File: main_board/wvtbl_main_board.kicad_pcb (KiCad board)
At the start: 2 copper layers, 29 x 110 mm, 11 parts, among them J101 V/Oct, J102 X, J103 Y, J104 Out, J105 Conn_02x08_Odd_Even

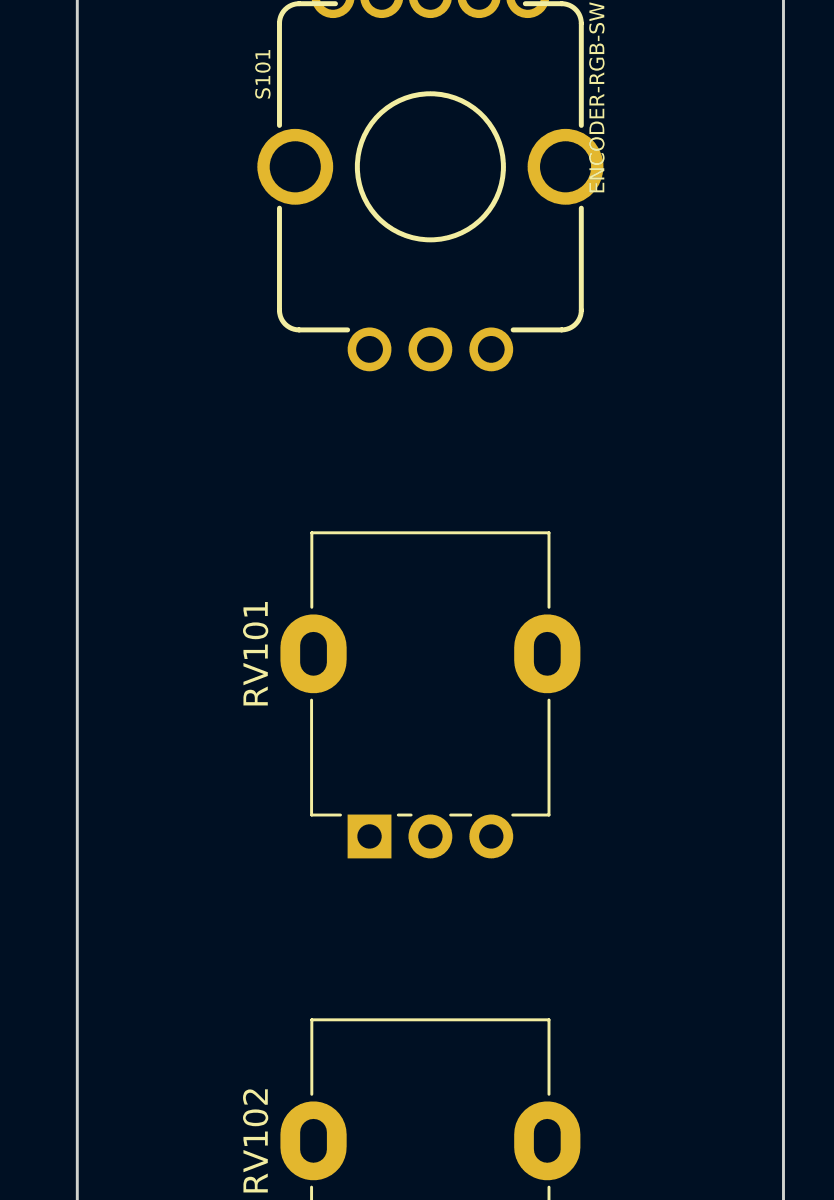
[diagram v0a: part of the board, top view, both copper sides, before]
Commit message: 6HP Compute module
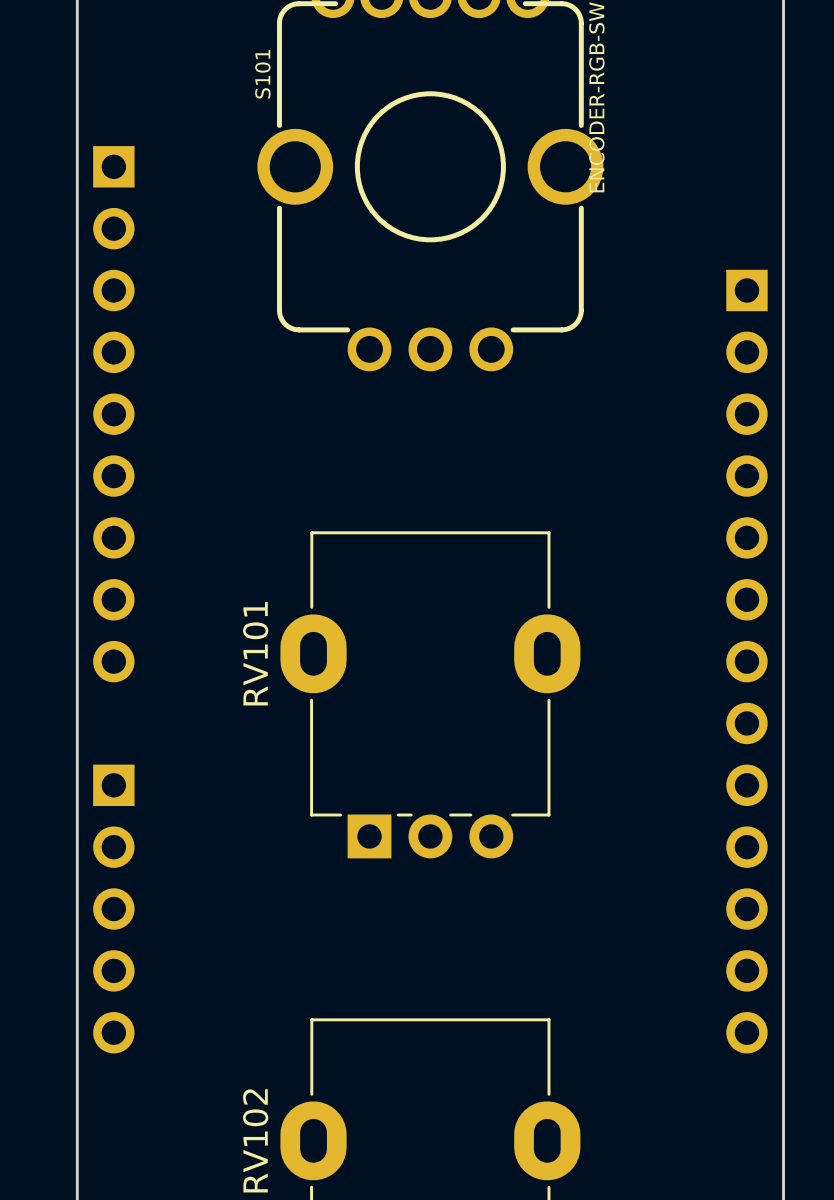
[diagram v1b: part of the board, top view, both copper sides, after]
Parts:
- added U101: CMPT6HP, WITNS:CMPT6HP, B.Cu at (50.0, 55.0)

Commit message: Main board PCB
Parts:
- removed J102: X, WITNS:Jack_3.5mm_QingPu_WQP-PJ398SM_Vertical_CircularHoles
- removed J103: Y, WITNS:Jack_3.5mm_QingPu_WQP-PJ398SM_Vertical_CircularHoles
- removed RV102, RV103, RV104: 100k, WITNS:Potentiometer_Alpha_RD901F-40-00D_Single_Vertical
- added C1: 10nF, Capacitor_SMD:C_0603_1608Metric, B.Cu at (44.0, 61.9)
- added C10: 10uF, Capacitor_SMD:CP_Elec_4x5.4, B.Cu at (42.0, 88.0)
- added C11: 100nF, Capacitor_SMD:C_0603_1608Metric, B.Cu at (45.8, 128.0)
- added C12: 10uF, Capacitor_SMD:CP_Elec_4x5.4, B.Cu at (42.0, 81.0)
- added C13: 100nF, Capacitor_SMD:C_0603_1608Metric, B.Cu at (50.8, 128.0)
- added C2: 100nF, Capacitor_SMD:C_0603_1608Metric, B.Cu at (50.8, 79.6)
- added C3: 100nF, Capacitor_SMD:C_0603_1608Metric, B.Cu at (59.0, 50.8)
- added C4: 10nF, Capacitor_SMD:C_0603_1608Metric, B.Cu at (51.6, 67.0)
- added C5: 100nF, Capacitor_SMD:C_0603_1608Metric, B.Cu at (50.8, 99.7)
- added C6: 100nF, Capacitor_SMD:C_0603_1608Metric, B.Cu at (43.3, 119.7)
- added C7: 100nF, Capacitor_SMD:C_0603_1608Metric, B.Cu at (58.2, 119.7)
- added C8: 10uF, Capacitor_SMD:CP_Elec_4x5.4, B.Cu at (38.0, 96.0)
- added C9: 100nF, Capacitor_SMD:C_0603_1608Metric, B.Cu at (50.8, 152.0)
- added D1: TVS 15V, Diode_SMD:D_SMA, B.Cu at (39.4, 144.0)
- added D2: TVS 15V, Diode_SMD:D_SMA, B.Cu at (39.4, 129.0)
- added D3: TVS 15V, Diode_SMD:D_SMA, B.Cu at (60.6, 144.0)
- added D4: TVS 15V, Diode_SMD:D_SMA, B.Cu at (60.6, 129.0)
- added J3: X, WITNS:Jack_3.5mm_QingPu_WQP-PJ398SM_Vertical_CircularHoles, F.Cu at (42.5, 132.0)
- added J4: Y, WITNS:Jack_3.5mm_QingPu_WQP-PJ398SM_Vertical_CircularHoles, F.Cu at (57.5, 132.0)
- added R1: 10k, Resistor_SMD:R_0603_1608Metric, B.Cu at (44.0, 59.9)
- added R2: 10k, Resistor_SMD:R_0603_1608Metric, B.Cu at (51.6, 65.0)
- added R3: 10k, Resistor_SMD:R_0603_1608Metric, B.Cu at (47.5, 59.0)
- added R4: 10k, Resistor_SMD:R_0603_1608Metric, B.Cu at (52.5, 59.0)
- added R5: 10k, Resistor_SMD:R_0603_1608Metric, B.Cu at (50.0, 51.0)
- added R6: 100R, Resistor_SMD:R_0603_1608Metric, B.Cu at (40.0, 66.8)
- added R7: 100R, Resistor_SMD:R_0603_1608Metric, B.Cu at (41.5, 66.8)
- added R8: 100R, Resistor_SMD:R_0603_1608Metric, B.Cu at (40.5, 72.8)
- added RV2: 100k, WITNS:Potentiometer_Alpha_RD901F-40-00D_Single_Vertical, F.Cu at (50.0, 95.0)
- added RV3: 100k, WITNS:Potentiometer_Alpha_RD901F-40-00D_Single_Vertical, F.Cu at (42.5, 115.0)
- added RV4: 100k, WITNS:Potentiometer_Alpha_RD901F-40-00D_Single_Vertical, F.Cu at (57.5, 115.0)
- J1: renamed from J105; value Conn_02x08_Odd_Even -> POWER
- renumbered J101 to J2, J104 to J5, RV101 to RV1, S101 to S1, U101 to U1
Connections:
- J1 pad 10: unconnected-(J105-Pad10) -> GND
- J1 pad 11: unconnected-(J105-Pad11) -> GND
- J1 pad 12: unconnected-(J105-Pad12) -> GND
- J1 pad 13: unconnected-(J105-Pad13) -> GND
- J1 pad 14: unconnected-(J105-Pad14) -> GND
- J1 pad 15: unconnected-(J105-Pad15) -> -12V
- J1 pad 16: unconnected-(J105-Pad16) -> -12V
- J1 pad 5: unconnected-(J105-Pad5) -> +5V
- J1 pad 6: unconnected-(J105-Pad6) -> +5V
- J1 pad 7: unconnected-(J105-Pad7) -> +12V
- J1 pad 8: unconnected-(J105-Pad8) -> +12V
- J1 pad 9: unconnected-(J105-Pad9) -> GND
- J2 pad S: unconnected-(J101-PadS) -> GND
- J2 pad T: unconnected-(J101-PadT) -> /CV1
- J2 pad TN: unconnected-(J101-PadTN) -> GND
- J5 pad S: unconnected-(J104-PadS) -> GND
- J5 pad T: unconnected-(J104-PadT) -> /OUT
- RV1 pad 1: unconnected-(RV101-Pad1) -> +3.3VA
- RV1 pad 2: unconnected-(RV101-Pad2) -> /POT_1
- RV1 pad 3: unconnected-(RV101-Pad3) -> GND
- S1 pad 1: unconnected-(S101-Pad1) -> Net-(R6-Pad1)
- S1 pad 2: unconnected-(S101-Pad2) -> Net-(R7-Pad1)
- S1 pad 3: unconnected-(S101-Pad3) -> /ENCODER_SWITCH
- S1 pad 4: unconnected-(S101-Pad4) -> Net-(R8-Pad1)
- S1 pad 5: unconnected-(S101-Pad5) -> +3.3V
- S1 pad A: unconnected-(S101-PadA) -> Net-(R1-Pad2)
- S1 pad B: unconnected-(S101-PadB) -> Net-(R2-Pad2)
- S1 pad C: unconnected-(S101-PadC) -> GND
- U1 pad 1: unconnected-(U101-Pad1) -> GND
- U1 pad 10: unconnected-(U101-Pad10) -> GND
- U1 pad 11: unconnected-(U101-Pad11) -> GND
- U1 pad 12: unconnected-(U101-Pad12) -> /OUT
- U1 pad 13: unconnected-(U101-Pad13) -> GND
- U1 pad 14: unconnected-(U101-Pad14) -> -12V
- U1 pad 15: unconnected-(U101-Pad15) -> GND
- U1 pad 16: unconnected-(U101-Pad16) -> +12V
- U1 pad 17: unconnected-(U101-Pad17) -> GND
- U1 pad 18: unconnected-(U101-Pad18) -> +5V
- U1 pad 19: unconnected-(U101-Pad19) -> GND
- U1 pad 2: unconnected-(U101-Pad2) -> /POT_1
- U1 pad 20: unconnected-(U101-Pad20) -> /LED_1
- U1 pad 21: unconnected-(U101-Pad21) -> /LED_2
- U1 pad 22: unconnected-(U101-Pad22) -> /LED_3
- U1 pad 23: unconnected-(U101-Pad23) -> GND
- U1 pad 24: unconnected-(U101-Pad24) -> /ENCODER_B
- U1 pad 25: unconnected-(U101-Pad25) -> /ENCODER_A
- U1 pad 26: unconnected-(U101-Pad26) -> /ENCODER_SWITCH
- U1 pad 27: unconnected-(U101-Pad27) -> +3.3V
- U1 pad 3: unconnected-(U101-Pad3) -> /POT_2
- U1 pad 4: unconnected-(U101-Pad4) -> /POT_3
- U1 pad 5: unconnected-(U101-Pad5) -> /POT_4
- U1 pad 6: unconnected-(U101-Pad6) -> +3.3VA
- U1 pad 7: unconnected-(U101-Pad7) -> /CV1
- U1 pad 8: unconnected-(U101-Pad8) -> /CV2
- U1 pad 9: unconnected-(U101-Pad9) -> /CV3
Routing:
- net +3.3VA: track 0.00 -> 92.4 mm
- net /CV1: track 0.00 -> 89.2 mm
- net -12V: track 0.00 -> 80.4 mm
- net +5V: track 0.00 -> 74.6 mm
- net +12V: track 0.00 -> 71.9 mm
- net /POT_3: track 0.00 -> 71.1 mm, vias 0 -> 1
- net /CV2: track 0.00 -> 67.8 mm
- net /OUT: track 0.00 -> 66.3 mm
- net /CV3: track 0.00 -> 60.7 mm
- net /POT_4: track 0.00 -> 55.7 mm
- net GND: track 0.00 -> 53.4 mm, vias 0 -> 62
- net /POT_2: track 0.00 -> 44.4 mm
- net Net-(R8-Pad1): track 0.00 -> 36.2 mm
- net +3.3V: track 0.00 -> 35.3 mm, vias 0 -> 2
- net /POT_1: track 0.00 -> 27.8 mm
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- added copper zone on B.Cu, net GND
- added copper zone on F.Cu, net GND
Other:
- board text added: "JLCJLCJLCJLC"
- board text added: "WITNS WVTBL v1.0 LFIACK"
